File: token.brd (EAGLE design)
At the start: 25 x 25 mm, 9 parts

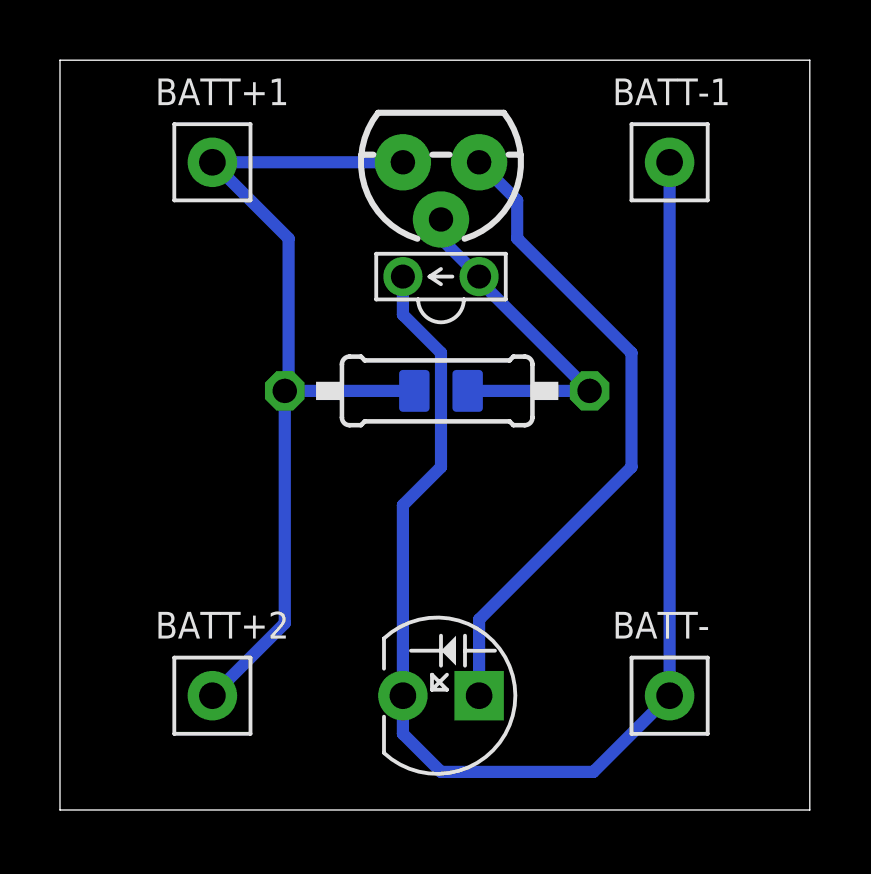
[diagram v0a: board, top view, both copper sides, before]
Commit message: Added hexagon outline
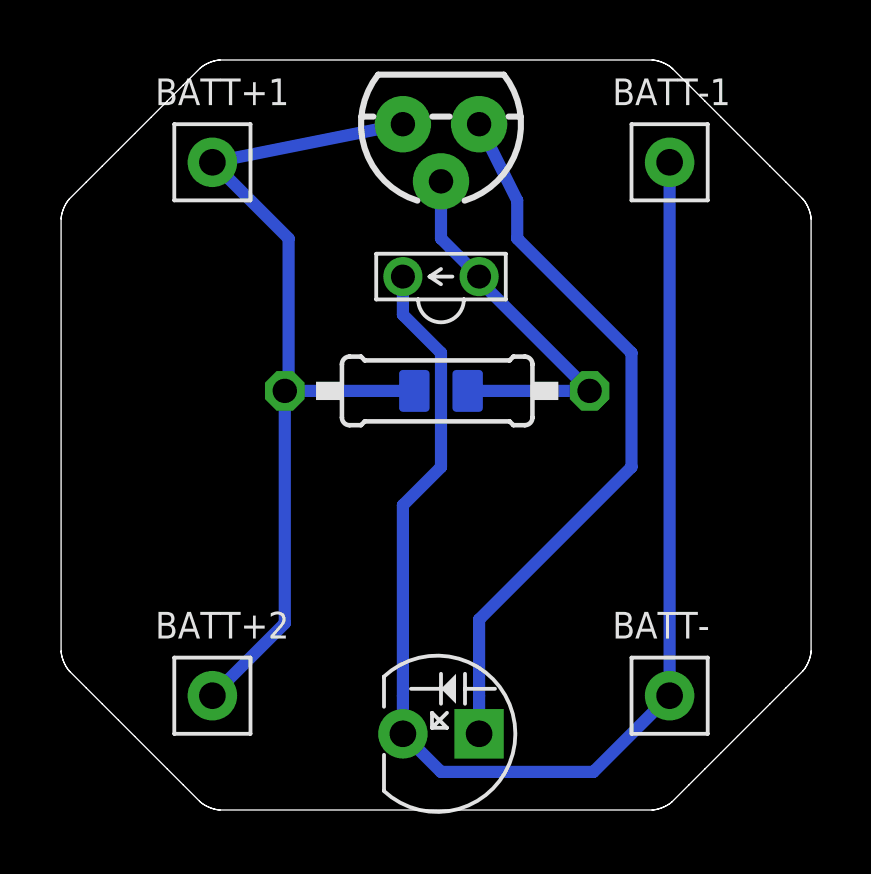
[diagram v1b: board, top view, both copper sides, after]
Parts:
- moved LED 1.27 mm to (12.7, 2.54)
- moved Q1 1.27 mm to (12.7, 22.9)
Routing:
- net N$1: track 22.0 -> 24.3 mm
- net N$2: track 11.8 -> 13.1 mm
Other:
- outline, holes or cut-outs redrawn
